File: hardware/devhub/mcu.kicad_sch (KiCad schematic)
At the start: 21 parts, among them J4 SWD, J9 UART debug, U3 STM32G0B1RET6

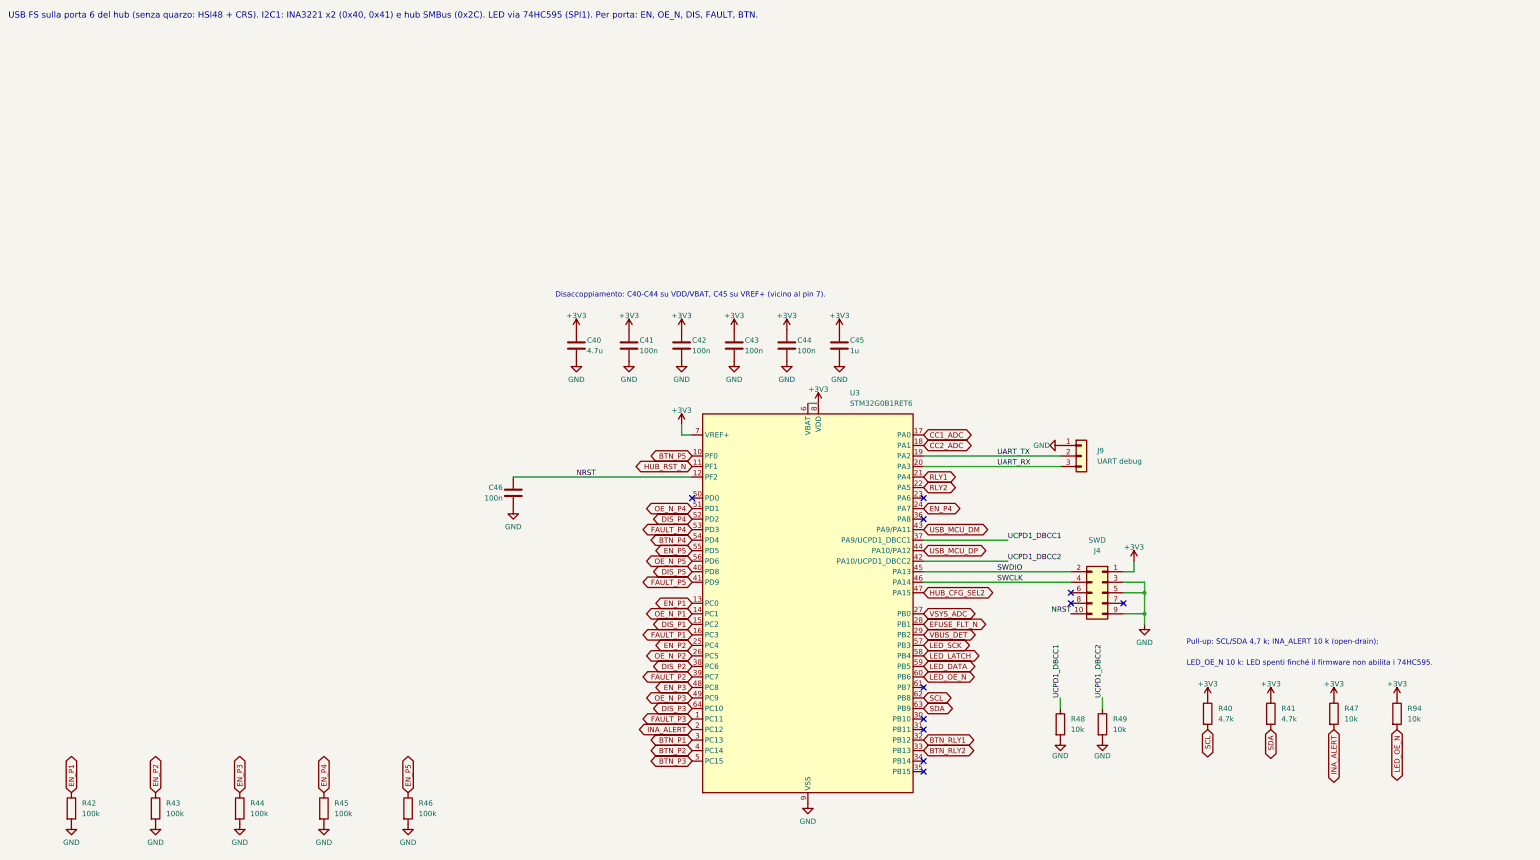
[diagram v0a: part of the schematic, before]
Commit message: Simplification: drop the 74HC595s, green LEDs on port EN, relay LEDs on relay commands (D38)
Red port LEDs and the host LED are driven by GPIOs that stay low in DFU; the power LED is on 3.3 V.
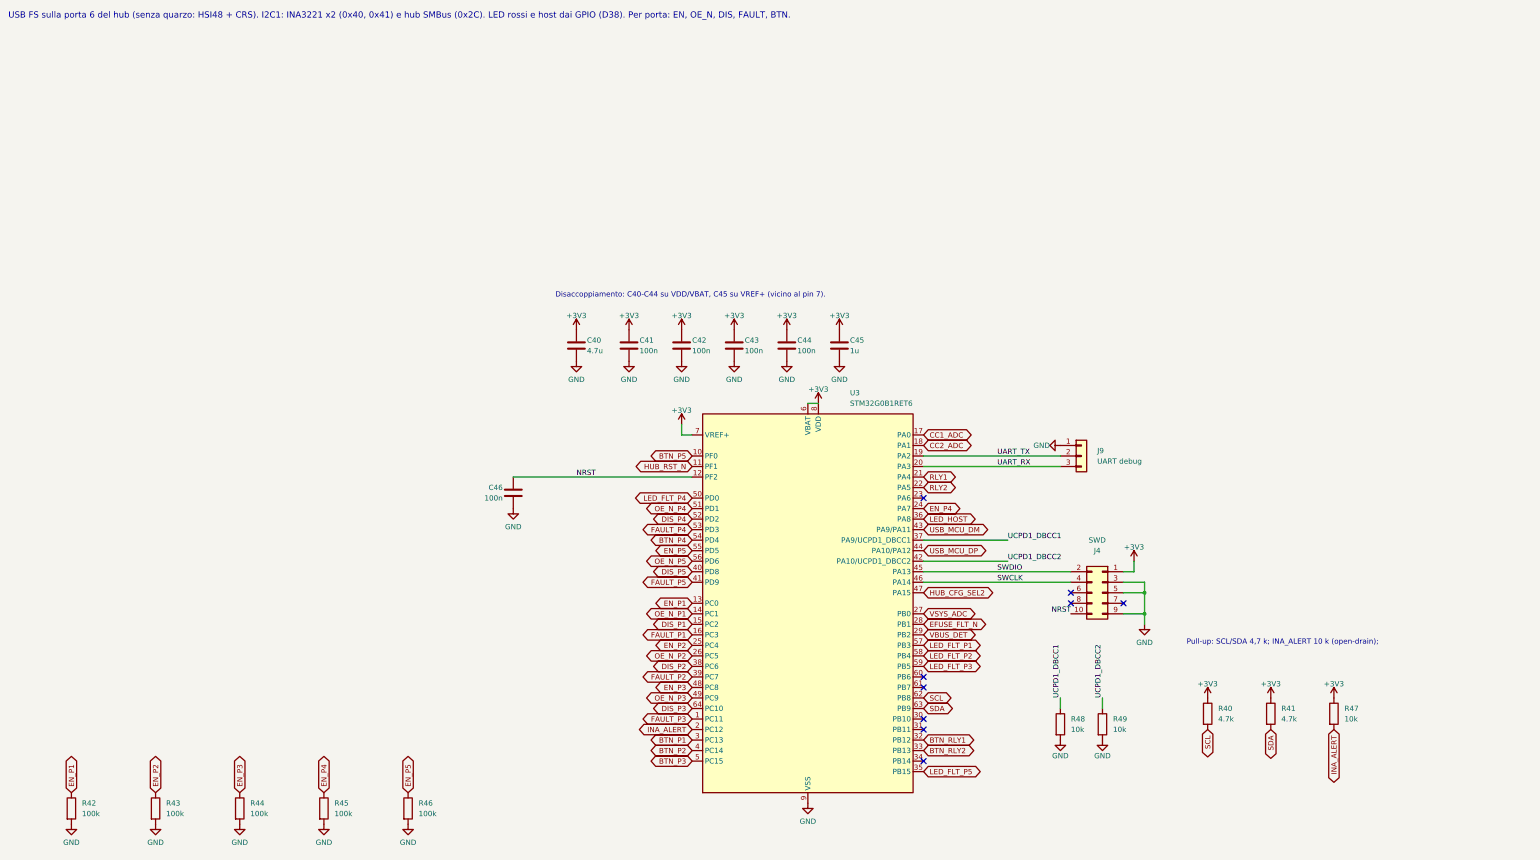
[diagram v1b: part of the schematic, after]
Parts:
- removed R94: 10k, Resistor_SMD:R_0603_1608Metric, symbol Device:R
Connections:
- net LED_FLT_P5: now reaches U3.35 (PB15)
- net LED_HOST: now reaches U3.36 (PA8)
- net LED_FLT_P4: now reaches U3.50 (PD0)
- net LED_DATA renamed LED_FLT_P3
- net LED_LATCH renamed LED_FLT_P2
- net LED_OE_N: no longer names the net of U3.60 (PB6)
- net LED_SCK renamed LED_FLT_P1
- no-connect marks 11 -> 9
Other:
- note added: "USB FS sulla porta 6 del hub (senza quarzo: HSI48 + CRS). I2C1: INA3221 x2 (0x40, 0x41) e hub SMBus (0x2C). LED rossi e host dai GPIO (D38). Per porta: EN, OE_N, DIS, FAULT, BTN."
- note removed: "LED_OE_N 10 k: LED spenti finché il firmware non abilita i 74HC595."
- note removed: "USB FS sulla porta 6 del hub (senza quarzo: HSI48 + CRS). I2C1: INA3221 x2 (0x40, 0x41) e hub SMBus (0x2C). LED via 74HC595 (SPI1). Per porta: EN, OE_N, DIS, FAULT, BTN."
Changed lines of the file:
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@@
 		)
 	)
-	(text "USB FS sulla porta 6 del hub (senza quarzo: HSI48 + CRS). I2C1: INA3221 x2 (0x40, 0x41) e hub SMBus (0x2C). LED via 74HC595 (SPI1). Per porta: EN, OE_N, DIS, FAULT, BTN."
+	(text "USB FS sulla porta 6 del hub (senza quarzo: HSI48 + CRS). I2C1: INA3221 x2 (0x40, 0x41) e hub SMBus (0x2C). LED rossi e host dai GPIO (D38). Per porta: EN, OE_N, DIS, FAULT, BTN."
 		(exclude_from_sim no)
 		(at 10.16 16.51 0)
@@
 		)
 	)
-	(text "LED_OE_N 10 k: LED spenti finché il firmware non abilita i 74HC595."
-		(exclude_from_sim no)
-		(at 294.64 172.72 0)
-		(effects
-			(font
-				(size 1.27 1.27)
-			)
-			(justify left bottom)
-		)
-	)
 	(text "R42-R46: pull-down sugli EN (porte spente al reset e durante il bootloader)."
 		(exclude_from_sim no)
@@
 	)
 	(no_connect
-		(at 231.14 198.12)
-	)
-	(no_connect
 		(at 231.14 195.58)
 	)
 	(no_connect
-		(at 231.14 137.16)
-	)
-	(no_connect
 		(at 231.14 185.42)
 	)
@@
 	)
 	(no_connect
-		(at 175.26 132.08)
-	)
-	(no_connect
 		(at 279.4 157.48)
 	)
@@
 		)
 	)
-	(global_label "LED_DATA"
+	(global_label "LED_FLT_P3"
 		(shape bidirectional)
 		(at 231.14 172.72 0)
@@
 		)
 	)
-	(global_label "LED_OE_N"
-		(shape bidirectional)
-		(at 231.14 175.26 0)
-		(fields_autoplaced yes)
-		(effects
-			(font
-				(size 1.27 1.27)
-			)
-			(justify left)
-		)
-		(property "Intersheetrefs" "${INTERSHEET_REFS}"
-			(at 231.14 175.26 0)
-			(hide yes)
-			(show_name no)
-			(do_not_autoplace no)
-			(effects
-				(font
-					(size 1.27 1.27)
-				)
-			)
-		)
-	)
 	(global_label "OE_N_P5"
 		(shape bidirectional)
@@
 		)
 	)
-	(global_label "LED_SCK"
+	(global_label "LED_FLT_P1"
 		(shape bidirectional)
 		(at 231.14 167.64 0)
@@
 		)
 	)
-	(global_label "LED_OE_N"
-		(shape bidirectional)
-		(at 345.44 187.96 270)
-		(fields_autoplaced yes)
-		(effects
-			(font
-				(size 1.27 1.27)
-			)
-			(justify right)
-		)
-		(property "Intersheetrefs" "${INTERSHEET_REFS}"
-			(at 345.44 187.96 0)
-			(hide yes)
-			(show_name no)
-			(do_not_autoplace no)
-			(effects
-				(font
-					(size 1.27 1.27)
-				)
-			)
-		)
-	)
-	(global_label "LED_LATCH"
+	(global_label "LED_FLT_P2"
 		(shape bidirectional)
 		(at 231.14 170.18 0)
@@
 		)
 	)
+	(no_connect
+		(at 231.14 175.26)
+	)
+	(global_label "LED_FLT_P4"
+		(shape bidirectional)
+		(at 175.26 132.08 180)
+		(fields_autoplaced yes)
+		(effects
+			(font
+				(size 1.27 1.27)
+			)
+			(justify right)
+		)
+		(property "Intersheetrefs" "${INTERSHEET_REFS}"
+			(at 175.26 132.08 0)
+			(hide yes)
+			(show_name no)
+			(do_not_autoplace no)
+			(effects
+				(font
+					(size 1.27 1.27)
+				)
+			)
+		)
+	)
+	(global_label "LED_FLT_P5"
+		(shape bidirectional)
+		(at 231.14 198.12 0)
+		(fields_autoplaced yes)
+		(effects
+			(font
+				(size 1.27 1.27)
+			)
+			(justify left)
+		)
+		(property "Intersheetrefs" "${INTERSHEET_REFS}"
+			(at 231.14 198.12 0)
+			(hide yes)
+			(show_name no)
+			(do_not_autoplace no)
+			(effects
+				(font
+					(size 1.27 1.27)
+				)
+			)
+		)
+	)
+	(global_label "LED_HOST"
+		(shape bidirectional)
+		(at 231.14 137.16 0)
+		(fields_autoplaced yes)
+		(effects
+			(font
+				(size 1.27 1.27)
+			)
+			(justify left)
+		)
+		(property "Intersheetrefs" "${INTERSHEET_REFS}"
+			(at 231.14 137.16 0)
+			(hide yes)
+			(show_name no)
+			(do_not_autoplace no)
+			(effects
+				(font
+					(size 1.27 1.27)
+				)
+			)
+		)
+	)
 	(symbol
 		(lib_id "Connector_Generic:Conn_02x05_Odd_Even")
@@
 	(symbol
 		(lib_id "power:+3V3")
-		(at 345.44 180.34 0)
-		(unit 1)
-		(body_style 1)
-		(exclude_from_sim no)
-		(in_bom yes)
-		(on_board yes)
-		(in_pos_files yes)
-		(dnp no)
-		(property "Reference" "#PWR103"
-			(at 345.44 180.34 0)
-			(hide yes)
-			(show_name no)
-			(do_not_autoplace no)
-			(effects
-				(font
-					(size 1.27 1.27)
-				)
-			)
-		)
-		(property "Value" "+3V3"
-			(at 345.44 176.94 0)
-			(show_name no)
-			(do_not_autoplace no)
-			(effects
-				(font
-					(size 1.27 1.27)
-				)
-			)
-		)
-		(property "Footprint" ""
-			(at 345.44 180.34 0)
-			(hide yes)
-			(show_name no)
-			(do_not_autoplace no)
-			(effects
-				(font
-					(size 1.27 1.27)
-				)
-			)
-		)
-		(property "Datasheet" ""
-			(at 345.44 180.34 0)
-			(hide yes)
-			(show_name no)
-			(do_not_autoplace no)
-			(effects
-				(font
-					(size 1.27 1.27)
-				)
-			)
-		)
-		(property "Description" ""
-			(at 345.44 180.34 0)
-			(hide yes)
-			(show_name no)
-			(do_not_autoplace no)
-			(effects
-				(font
-					(size 1.27 1.27)
-				)
-			)
-		)
-		(pin "1"
-		)
-		(instances
-			(project "devhub"
-				(path "/af6ea7d8-d1ba-5fc6-aec8-abf514847630/357eb134-3b36-5717-b194-1b0e8ceb4547"
-					(reference "#PWR103")
-					(unit 1)
-				)
-			)
-		)
-	)
-	(symbol
-		(lib_id "power:+3V3")
 		(at 330.2 180.34 0)
 		(unit 1)
@@
 					(unit 1)
 				)
-			)
-		)
-	)
-	(symbol
-		(lib_id "Device:R")
-		(at 345.44 184.15 0)
-		(unit 1)
-		(body_style 1)
-		(exclude_from_sim no)
-		(in_bom yes)
-		(on_board yes)
-		(in_pos_files yes)
-		(dnp no)
-		(property "Reference" "R94"
-			(at 347.98 182.88 0)
-			(show_name no)
-			(do_not_autoplace no)
-			(effects
-				(font
-					(size 1.27 1.27)
-				)
-				(justify left)
-			)
-		)
-		(property "Value" "10k"
-			(at 347.98 185.42 0)
-			(show_name no)
-			(do_not_autoplace no)
-			(effects
-				(font
-					(size 1.27 1.27)
-				)
-				(justify left)
-			)
-		)
-		(property "Footprint" "Resistor_SMD:R_0603_1608Metric"
-			(at 345.44 184.15 0)
-			(hide yes)
-			(show_name no)
-			(do_not_autoplace no)
-			(effects
-				(font
-					(size 1.27 1.27)
-				)
-			)
-		)
-		(property "Datasheet" ""
-			(at 345.44 184.15 0)
-			(hide yes)
-			(show_name no)
-			(do_not_autoplace no)
-			(effects
-				(font
-					(size 1.27 1.27)
-				)
-			)
-		)
-		(property "Description" "Resistor"
-			(at 345.44 184.15 0)
-			(hide yes)
-			(show_name no)
-			(do_not_autoplace no)
-			(effects
-				(font
-					(size 1.27 1.27)
-				)
-			)
-		)
-		(pin "1"
-		)
-		(pin "2"
-		)
-		(instances
-			(project "devhub"
-				(path "/af6ea7d8-d1ba-5fc6-aec8-abf514847630/357eb134-3b36-5717-b194-1b0e8ceb4547"
-					(reference "R94")
-					(unit 1)
-				)

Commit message: Simplification: input shunt moved after the eFuse, VSYS_ADC divider removed (D40)
The INA3221 is no longer exposed to the supply voltage and reads 5V_SYS; LOCAL_PWR gets a 10k pull-up (R26). Push-button capacitors kept (D39).
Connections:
- net VSYS_ADC: no longer names the net of U3.27 (PB0)
- no-connect marks 9 -> 10
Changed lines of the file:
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@@
-		)
-	)
-	(global_label "VSYS_ADC"
-		(shape bidirectional)
-		(at 231.14 160.02 0)
-		(fields_autoplaced yes)
-		(effects
-			(font
-				(size 1.27 1.27)
-			)
-			(justify left)
-		)
-		(property "Intersheetrefs" "${INTERSHEET_REFS}"
-			(at 231.14 160.02 0)
-			(hide yes)
-			(show_name no)
-			(do_not_autoplace no)
-			(effects
-				(font
-					(size 1.27 1.27)
-				)
-			)
 		)
 	)
@@
 		(at 231.14 175.26)
 	)
+	(no_connect
+		(at 231.14 160.02)
+	)
 	(global_label "LED_FLT_P4"

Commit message: PCB rules in KiCad, USB pair names, eFuse output bypass and U2 thermal vias (D44-D50)
Stackup JLC04161H-7628, netclasses and custom DRC rules (devhub.kicad_dru) from
docs/regole-pcb.md, with a section for the checks that DRC cannot cover. C7 1 uF on
the TPS259470A output before the shunt (D48). USB nets renamed to DP/DN so KiCad
recognizes the differential pairs (D49). U2 footprint with 0.3 mm thermal vias, open
on both sides for the prototype; encroached vias and a JLCPCB order note for
production (D50). Also includes stock part codes, cost comparison and placement rules
(D44-D47).
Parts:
- C40: digikey (none) -> 1276-1784-1-ND; lcsc (none) -> C19666; mouser (none) -> 187-CL10A475KO8NNNC; warehouse (none) -> 276
- C41, C42, C43, C44, C46: digikey (none) -> 1276-1000-1-ND; lcsc (none) -> C1591; mouser (none) -> 187-CL10B104KB8NNNC; warehouse (none) -> 235
- C45: digikey (none) -> 1276-1184-1-ND; lcsc (none) -> C29936; mouser (none) -> 187-CL10B105KA8NNNC; warehouse (none) -> 240
- J4: digikey (none) -> SAM8799-ND; lcsc (none) -> C5155080; mouser (none) -> 200-FTSH10501LDVK
- J9: digikey (none) -> 732-5316-ND; lcsc (none) -> C49257; mouser (none) -> 710-61300311121
- R40, R41: digikey (none) -> 311-4.70KHRCT-ND; lcsc (none) -> C99782; mouser (none) -> 603-RC0603FR-074K7L
- R42, R43, R44, R45, R46: digikey (none) -> 311-100KHRCT-ND; lcsc (none) -> C2906980; mouser (none) -> 603-RC0603FR-07100KL; warehouse (none) -> 247
- R47, R48, R49: digikey (none) -> 311-10.0KHRCT-ND; lcsc (none) -> C2906982; mouser (none) -> 603-RC0603FR-0710KL; warehouse (none) -> 248
- U3: digikey (none) -> 497-STM32G0B1RET6-ND; lcsc (none) -> C2829307; mouser (none) -> 511-STM32G0B1RET6
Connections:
- net USB_MCU_DM renamed USB_MCU_DN

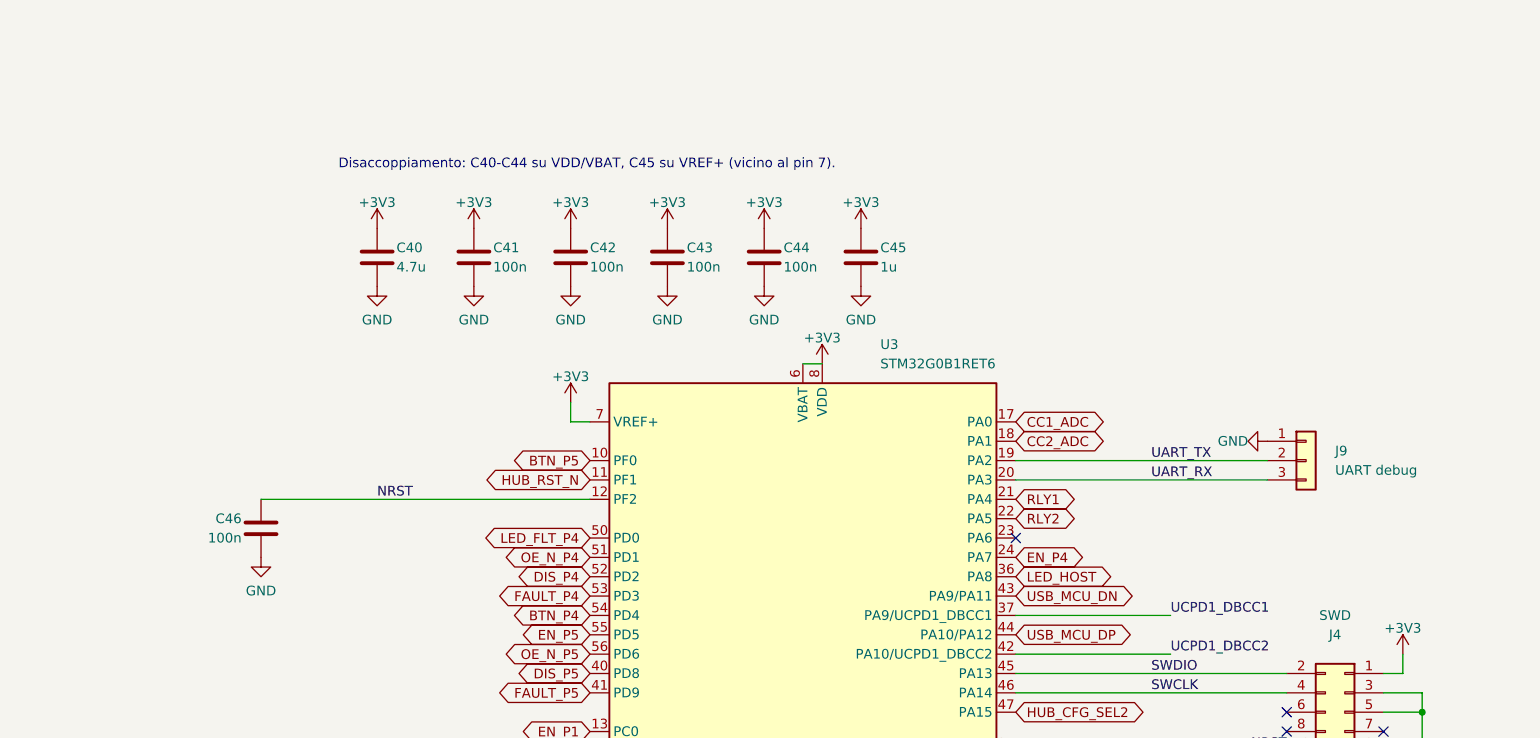
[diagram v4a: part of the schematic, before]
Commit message: MCU and hub decoupling, USB2517 checklist, VBUS_DET without clamp diode (D53, D57, D58)
- MCU U3 decoupling per DS13560 fig. 15: C41 100 nF + C40 4.7 uF on VDD/VSS,
  C42 100 nF on VREF+; C43, C44 and C45 removed (D57).
- Hub U2 decoupling per the Microchip USB2517 Hardware Design Checklist: 100 nF on
  each 3.3 V pin (C38 added), 1 uF shared by VDDA33 (C31) and on VDD33CR, only 1 uF
  on VDD18 and VDD18PLL (C34, C36 removed). Each capacitor drawn on its pin's wire.
  The 100 nF of U2 and U12 are 0402 (stock ID 217) to fit next to the pins between
  the USB pairs; DRC exception for the +3V3 stubs inside the U2_DECAP areas (D58).
- VBUS_DET: D21 removed, plain 100k/100k divider as recommended by the checklist
  (D53, R03-02 closed).
- USB-C connector exits without tuning meanders: the ~2.3 mm D+/D- difference of the
  pad crossing is accepted; looser skew limit on the connector-side nets.
- PCB: relay contact keepouts redrawn, U2 fanout and decoupling placement, zone refill.
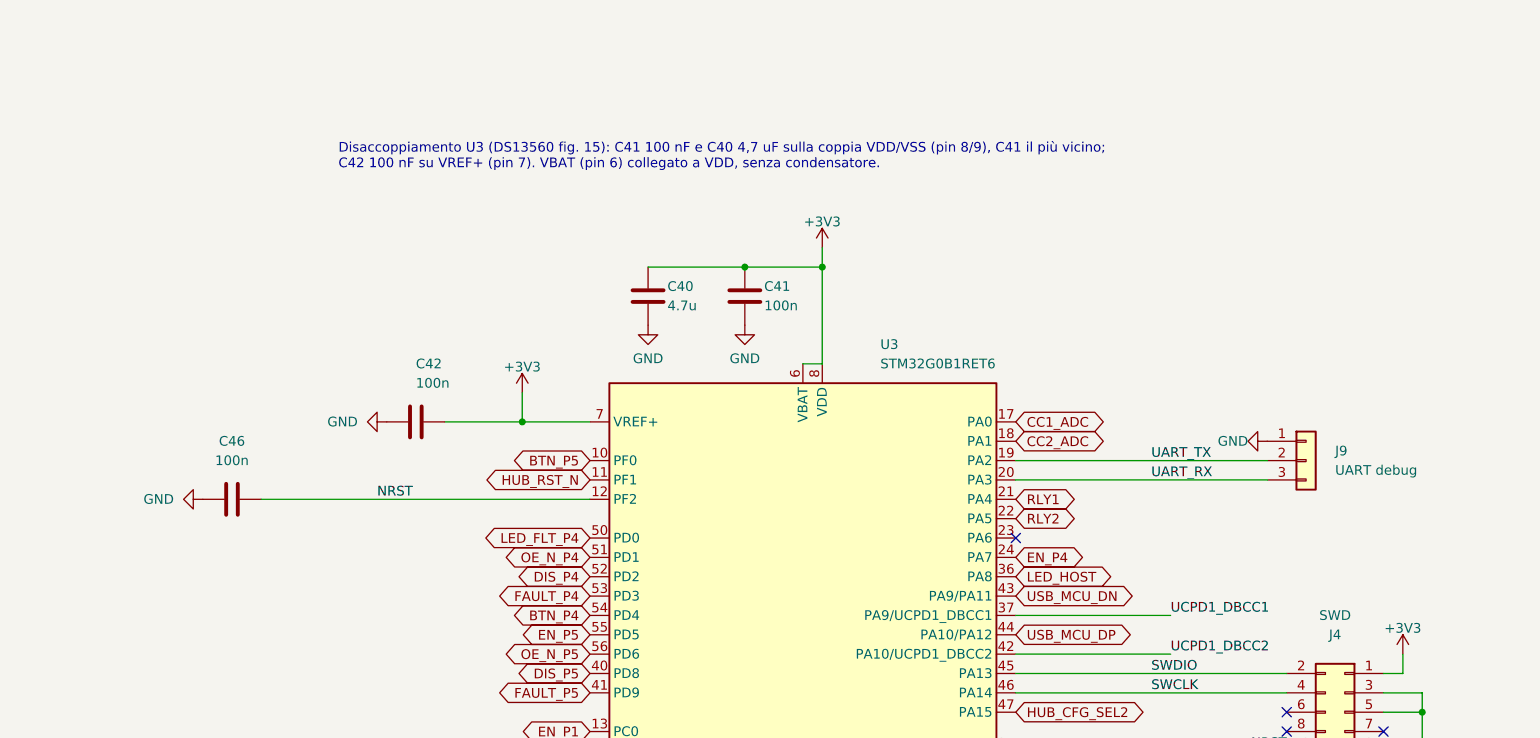
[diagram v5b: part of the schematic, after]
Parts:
- removed C43, C44: 100n, Capacitor_SMD:C_0603_1608Metric, symbol Device:C
- removed C45: 1u, Capacitor_SMD:C_0603_1608Metric, symbol Device:C
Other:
- note added: "Disaccoppiamento U3 (DS13560 fig. 15): C41 100 nF e C40 4,7 uF sulla coppia VDD/VSS (pin 8/9), C41 il più vicino; C42 100 nF su VREF+ (pin 7). VBAT (pin 6) collegato a VDD, senza condensatore."
- note removed: "Disaccoppiamento: C40-C44 su VDD/VBAT, C45 su VREF+ (vicino al pin 7)."
- moved on the sheet: C40, C41, C42, C46
